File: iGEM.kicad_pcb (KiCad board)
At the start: 4 copper layers, 98 x 98 mm, 61 parts, among them IC1 TMCS1107A1BQDRQ1, IC2 MCP4642-502E_UN, IC3 SN74LVC2G08IDCTRQ1, J1 COIL, J2 Conn_01x03, J3 Conn_01x02, J4 Conn_01x03, J5 Conn_01x03, J6 Conn_02x03_Odd_Even, M1 Fan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

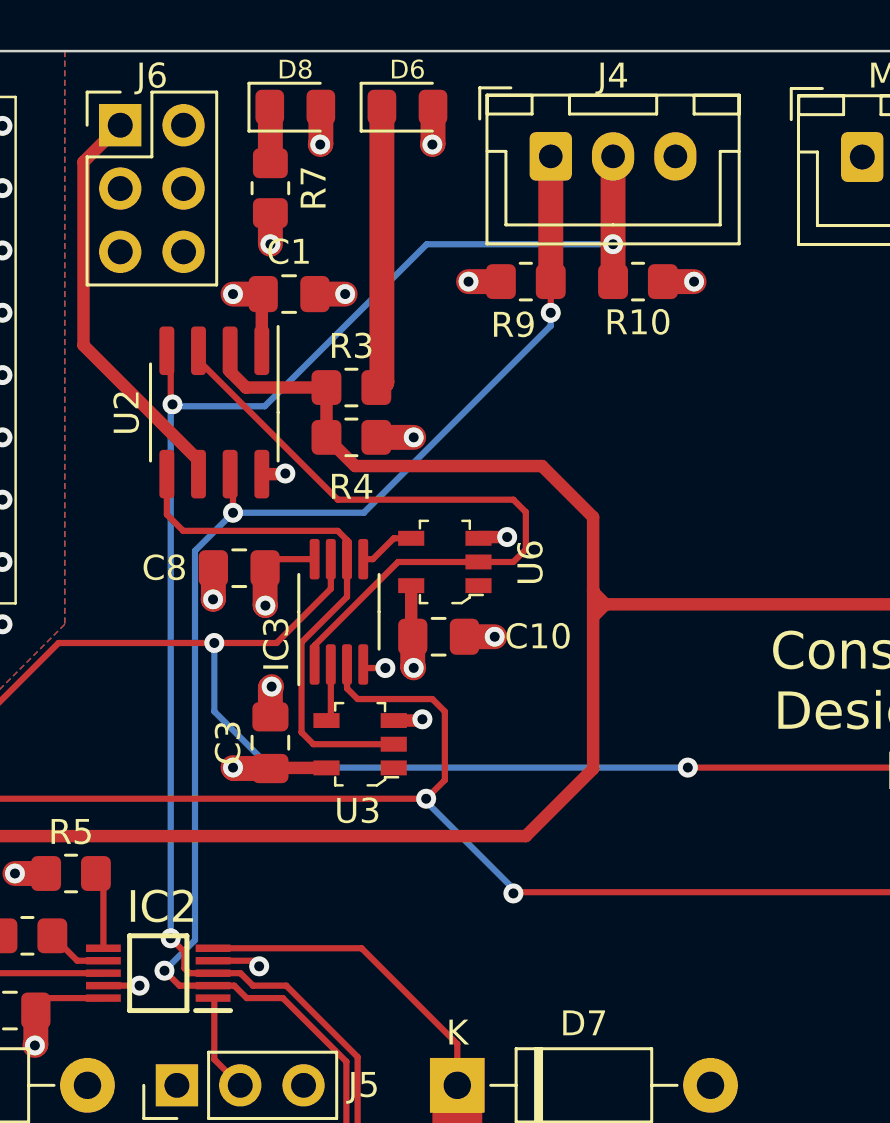
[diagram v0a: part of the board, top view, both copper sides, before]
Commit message: Adding level shifter
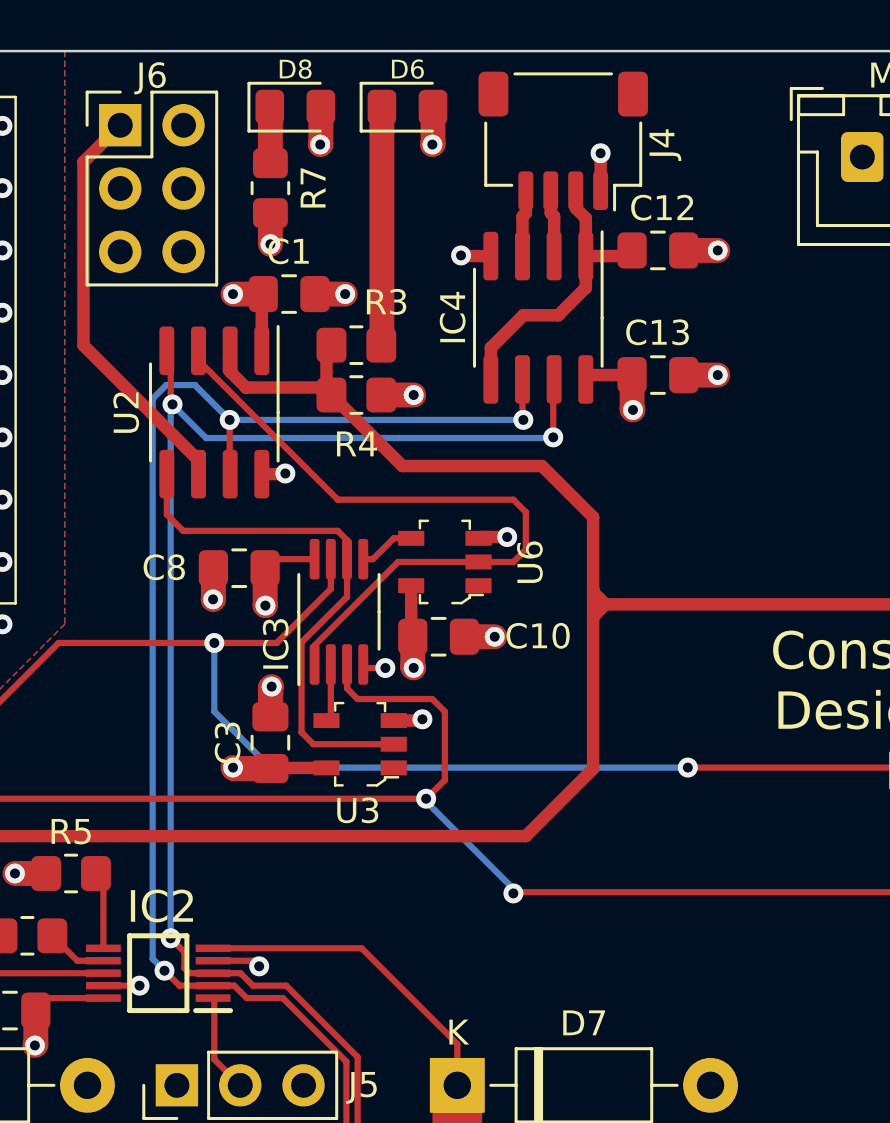
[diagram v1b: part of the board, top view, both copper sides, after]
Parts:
- removed R10, R9: 4.7K, Resistor_SMD:R_0805_2012Metric_Pad1.20x1.40mm_HandSolder
- added C12: 0.1 uF, Capacitor_SMD:C_0805_2012Metric_Pad1.18x1.45mm_HandSolder, F.Cu at (123.8, 55.0)
- added C13: 0.1 uF, Capacitor_SMD:C_0805_2012Metric_Pad1.18x1.45mm_HandSolder, F.Cu at (123.8, 60.0)
- added IC4: NLSX4373DR2G, Package_SO:SOIC-8_3.9x4.9mm_P1.27mm, F.Cu at (119.0, 57.7)
- J4: value Conn_01x03 -> Conn_01x04; footprint Connector_JST:JST_XH_B3B-XH-A_1x03_P2.50mm_Vertical -> Connector_JST:JST_SH_SM04B-SRSS-TB_1x04-1MP_P1.00mm_Horizontal
- moved R3 1.71 mm to (111.7, 58.8)
- moved R4 1.71 mm to (111.7, 60.8)
- moved J4 0.80 mm to (120.0, 50.6), turned to 180 degrees
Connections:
- J4 pad 1: SCL -> GND
- J4 pad 2: SDA -> VCC
- J4 pad 3: GND -> SDA-LOW
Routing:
- net VCC: track 0.00 -> 12.1 mm
- net SDA: track 88.6 -> 81.3 mm
- net GND: track 30.5 -> 35.7 mm, vias 116 -> 120
- net SDA-LOW: track 0.00 -> 2.68 mm
- net SCL-LOW: track 0.00 -> 2.68 mm
- net Net-(D6-Pad1): track 11.3 -> 9.56 mm
- net ENABLE: track 169.5 -> 170.5 mm
- net SCL: track 84.8 -> 83.8 mm
- net +5V: track 40.5 -> 41.3 mm, vias 75 -> 74

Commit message: Added useful silk and moved fan connector
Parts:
- moved M1 15.5 mm to (147.5, 50.5)
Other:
- board text added: "+"
- board text added: "+5V"
- board text added: "-"
- board text added: "1"
- board text added: "2"
- board text added: "A0"
- board text added: "ADDR"
- board text added: "COIL"
- board text added: "FAN"
- board text added: "GND"
- board text added: "STEMMA QT"
- board text added: "UPDI"
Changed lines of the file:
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@@
     (property "Sheetname" "")
     (attr through_hole)
-    (fp_text reference "J1" (at 2.54 -5.08) (layer "F.SilkS")
+    (fp_text reference "J1" (at 0.08 -4.75) (layer "F.SilkS")
       (effects (font (size 1 1) (thickness 0.15)))
     )
@@
     (property "Sheetname" "")
     (attr smd)
-    (fp_text reference "J4" (at -4 -0.1 90) (layer "F.SilkS")
+    (fp_text reference "J4" (at -5 -0.1 180) (layer "F.SilkS")
       (effects (font (size 1 1) (thickness 0.15)))
     )
@@
   )
   (footprint "Connector_JST:JST_XH_B2B-XH-A_1x02_P2.50mm_Vertical" (layer "F.Cu")
-    (at 132 51.25)
+    (at 147.5 50.475)
     (descr "JST XH series connector, B2B-XH-A (http://www.jst-mfg.com/product/pdf/eng/eXH.pdf), generated with kicad-footprint-generator")
     (tags "connector JST XH vertical")
@@
     (property "Sheetname" "")
     (attr through_hole)
-    (fp_text reference "M1" (at 1.25 -3.25) (layer "F.SilkS")
+    (fp_text reference "M1" (at 1.25 4.775) (layer "F.SilkS")
       (effects (font (size 1 1) (thickness 0.15)))
     )
@@
     (property "exclude_from_bom" "")
     (attr through_hole exclude_from_bom)
-    (fp_text reference "J6" (at 1.275 -1.975) (layer "F.SilkS")
+    (fp_text reference "J6" (at -0.225 -1.975) (layer "F.SilkS")
       (effects (font (size 1 1) (thickness 0.15)))
     )
@@
   (gr_line (start 63 141) (end 63 51) (layer "Edge.Cuts") (width 0.1))
   (gr_line (start 161 51) (end 161 141) (layer "Edge.Cuts") (width 0.1))
+  (gr_text "ADDR" (at 110.25 110.75) (layer "B.SilkS")
+    (effects (font (size 1 1) (thickness 0.15)) (justify mirror))
+  )
+  (gr_text "+5V" (at 106.75 50 -90) (layer "B.SilkS")
+    (effects (font (size 0.5 0.5) (thickness 0.1)) (justify mirror))
+  )
+  (gr_text "GND" (at 106.75 55 -90) (layer "B.SilkS")
+    (effects (font (size 0.5 0.5) (thickness 0.1)) (justify mirror))
+  )
+  (gr_text "A0" (at 107 86.5) (layer "B.SilkS")
+    (effects (font (size 1 1) (thickness 0.15)) (justify mirror))
+  )
+  (gr_text "UPDI" (at 105 48) (layer "B.SilkS")
+    (effects (font (size 1 1) (thickness 0.15)) (justify mirror))
+  )
+  (gr_text "1" (at 109.5 143.75) (layer "B.SilkS")
+    (effects (font (size 1.5 1.5) (thickness 0.25)) (justify mirror))
+  )
+  (gr_text "GND" (at 110.25 108.25) (layer "B.SilkS")
+    (effects (font (size 1 1) (thickness 0.15)) (justify mirror))
+  )
+  (gr_text "+" (at 81.5 51) (layer "B.SilkS")
+    (effects (font (size 5 5) (thickness 0.5)))
+  )
+  (gr_text "UPDI" (at 100.25 50 -90) (layer "B.SilkS")
+    (effects (font (size 0.5 0.5) (thickness 0.1)) (justify mirror))
+  )
+  (gr_text "+5V" (at 109.75 86.5) (layer "B.SilkS")
+    (effects (font (size 1 1) (thickness 0.15)) (justify mirror))
+  )
+  (gr_text "+5V" (at 110.25 113.25) (layer "B.SilkS")
+    (effects (font (size 1 1) (thickness 0.15)) (justify mirror))
+  )
+  (gr_text "2" (at 114.5 143.75) (layer "B.SilkS")
+    (effects (font (size 1.5 1.5) (thickness 0.25)) (justify mirror))
+  )
+  (gr_text "-" (at 93.5 51) (layer "B.SilkS")
+    (effects (font (size 5 5) (thickness 0.5)))
+  )
+  (gr_text "GND" (at 104.25 86.5) (layer "B.SilkS")
+    (effects (font (size 1 1) (thickness 0.15)) (justify mirror))
+  )
+  (gr_text "A0" (at 107 86.5) (layer "F.SilkS")
+    (effects (font (size 1 1) (thickness 0.15)))
+  )
+  (gr_text "COIL" (at 112.5 136) (layer "F.SilkS")
+    (effects (font (size 1 1) (thickness 0.15)))
+  )
+  (gr_text "GND" (at 106.75 55 90) (layer "F.SilkS")
+    (effects (font (size 0.5 0.5) (thickness 0.1)))
+  )
+  (gr_text "+5V" (at 109.75 86.5) (layer "F.SilkS")
+    (effects (font (size 1 1) (thickness 0.15)))
+  )
+  (gr_text "+5V" (at 106.75 50 90) (layer "F.SilkS")
+    (effects (font (size 0.5 0.5) (thickness 0.1)))
+  )
+  (gr_text "+" (at 71.5 49) (layer "F.SilkS")
+    (effects (font (size 2.5 2.5) (thickness 0.15)))
+  )
+  (gr_text "UPDI" (at 100.25 50 90) (layer "F.SilkS")
+    (effects (font (size 0.5 0.5) (thickness 0.1)))
+  )
+  (gr_text "-" (at 99.5 48.25) (layer "F.SilkS")
+    (effects (font (size 2.5 2.5) (thickness 0.15)))
+  )
+  (gr_text "GND" (at 110.25 108.25) (layer "F.SilkS")
+    (effects (font (size 1 1) (thickness 0.15)))
+  )
+  (gr_text "FAN" (at 141 49.25) (layer "F.SilkS")
+    (effects (font (size 2.5 2.5) (thickness 0.5)))
+  )
+  (gr_text "STEMMA QT" (at 128.25 48.5) (layer "F.SilkS")
+    (effects (font (size 1 1) (thickness 0.15)))
+  )
+  (gr_text "2" (at 118 144.25) (layer "F.SilkS")
+    (effects (font (size 1 1) (thickness 0.15)))
+  )
+  (gr_text "UPDI" (at 105 48) (layer "F.SilkS")
+    (effects (font (size 1 1) (thickness 0.15)))
+  )
+  (gr_text "GND" (at 104.25 86.5) (layer "F.SilkS")
+    (effects (font (size 1 1) (thickness 0.15)))
+  )
+  (gr_text "+5V" (at 110.25 113.25) (layer "F.SilkS")
+    (effects (font (size 1 1) (thickness 0.15)))
+  )
+  (gr_text "ADDR" (at 110.25 110.75) (layer "F.SilkS")
+    (effects (font (size 1 1) (thickness 0.15)))
+  )
   (gr_text "Constant Current Coil Driver\nDesign by Sreenivas Eadara\nHopkins iGEM 2021" (at 142.9 73.5) (layer "F.SilkS")
     (effects (font (size 1.5 1.5) (thickness 0.3)))
   )
+  (gr_text "1" (at 106 144) (layer "F.SilkS")
+    (effects (font (size 1 1) (thickness 0.15)))
+  )
   (segment (start 99.3375 85) (end 101.55 85) (width 0.25) (layer "F.Cu") (net 1))

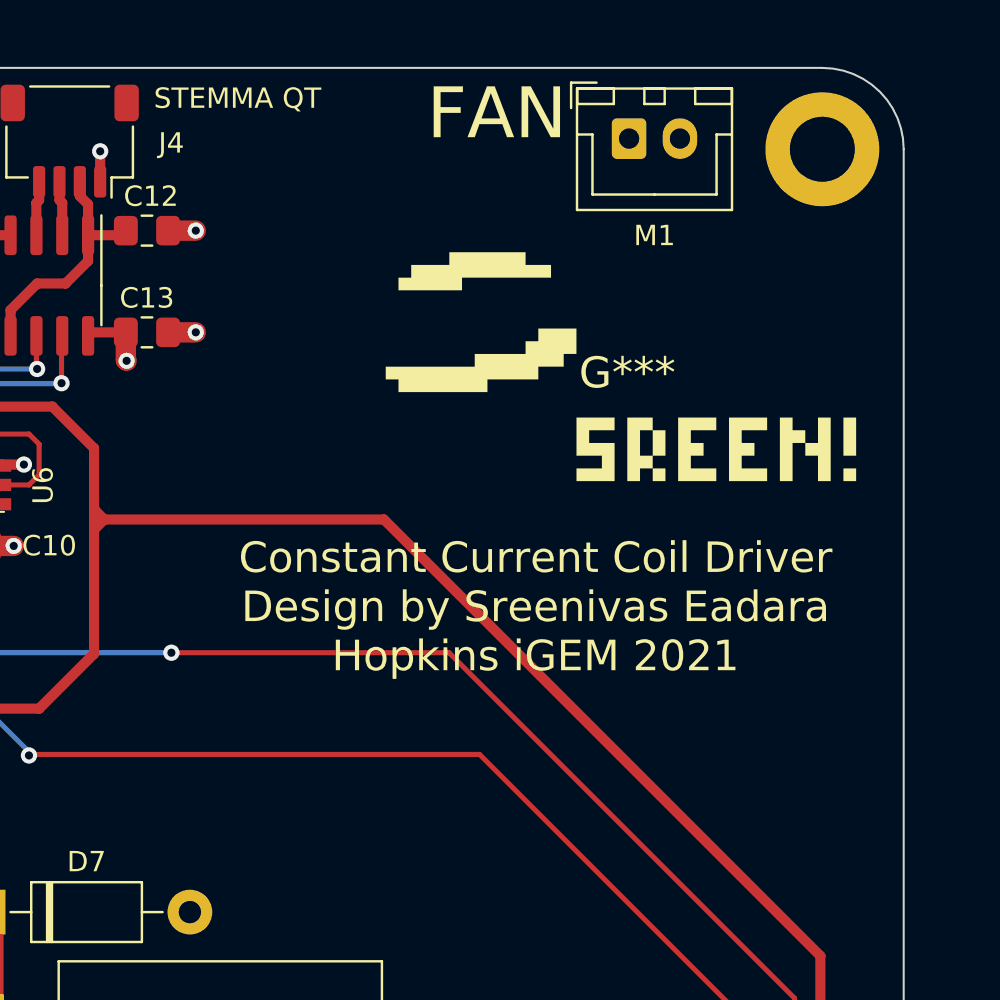
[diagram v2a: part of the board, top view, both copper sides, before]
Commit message: Adding inductor to prevent fan voltage spikes
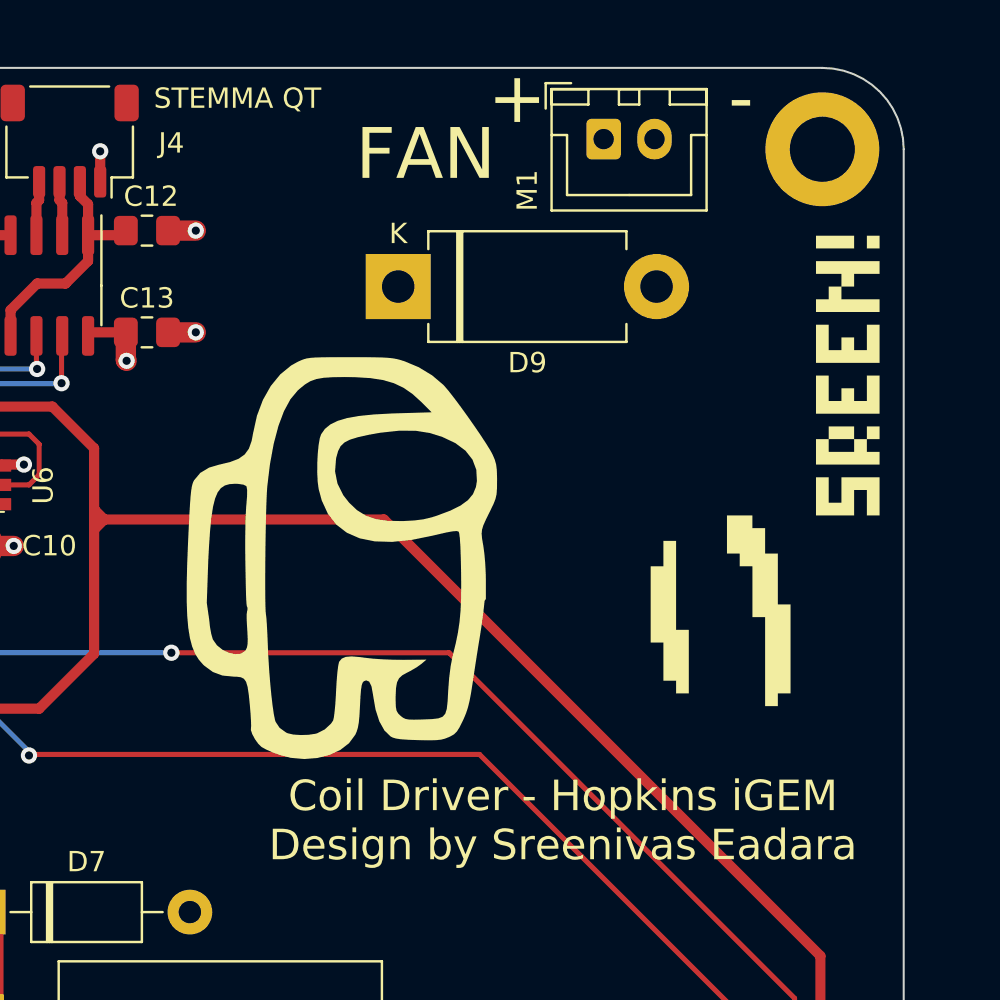
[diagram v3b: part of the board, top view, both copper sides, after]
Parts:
- added D9: SB2060, Diode_THT:D_DO-201AD_P12.70mm_Horizontal, F.Cu at (136.2, 57.8)
- G***: moved to F.Cu
- moved G*** 10.9 mm to (133.9, 71.0), turned to 0 degrees
- moved G*** 8.40 mm to (154.5, 66.5), turned to 90 degrees
- moved M1 1.25 mm to (146.2, 50.5)
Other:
- board text added: "Coil Driver - Hopkins iGEM Design by Sreenivas Eadara"
- board text removed: "Constant Current Coil Driver Design by Sreenivas Eadara Hopkins iGEM 2021"

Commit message: Adding programming power protection
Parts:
- moved C13 2.20 mm to (123.8, 62.2)
- moved IC4 2.10 mm to (119.0, 59.8)
- moved C10 2.01 mm to (116.8, 71.4)
- moved C12 1.55 mm to (122.2, 55.0)
- moved U6 0.75 mm to (114.8, 68.1), turned to 180 degrees
- moved C11 0.25 mm to (97.8, 85.8)
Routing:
- net PWM1: track 28.0 -> 22.1 mm
- net SDA-LOW: track 2.68 -> 4.78 mm
- net SCL-LOW: track 2.68 -> 4.78 mm
- net Net-(IC3-Pad5): track 2.27 -> 3.42 mm
- net ENABLE: track 170.5 -> 169.3 mm
- net SDA: track 81.3 -> 82.5 mm
- net SCL: track 83.8 -> 84.7 mm
- net GND: track 35.7 -> 36.3 mm
